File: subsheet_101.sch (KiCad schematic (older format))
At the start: 6 parts, among them U101 ST_BLITTER_PHY

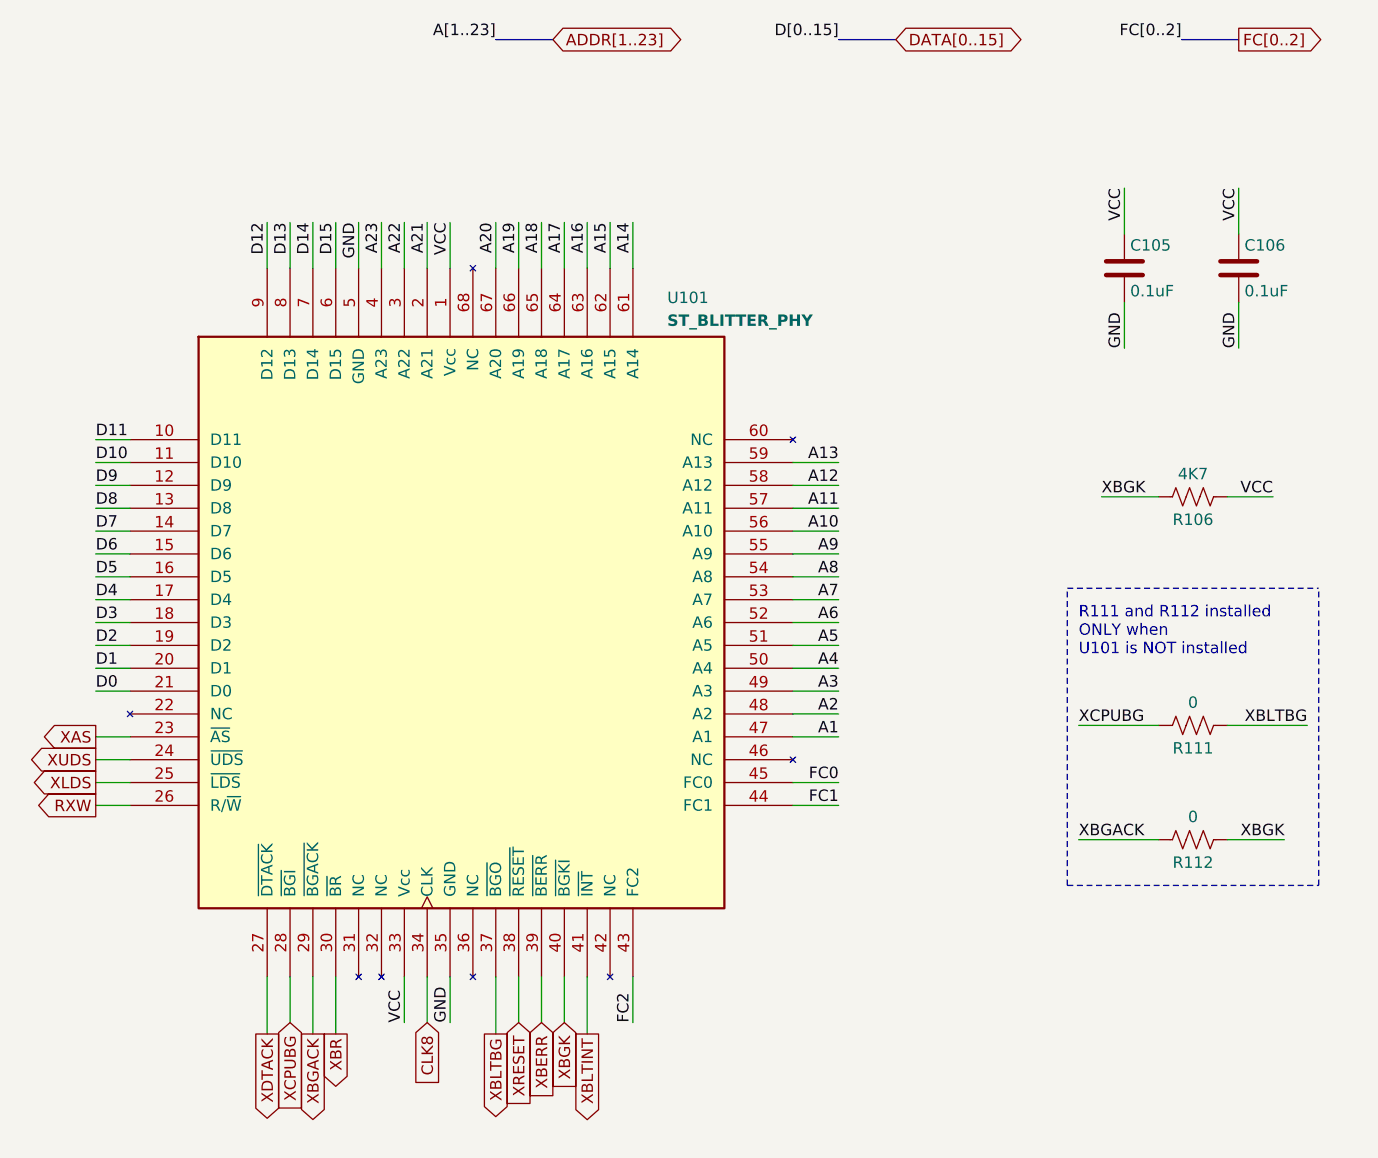
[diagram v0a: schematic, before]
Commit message: removed the external blitter
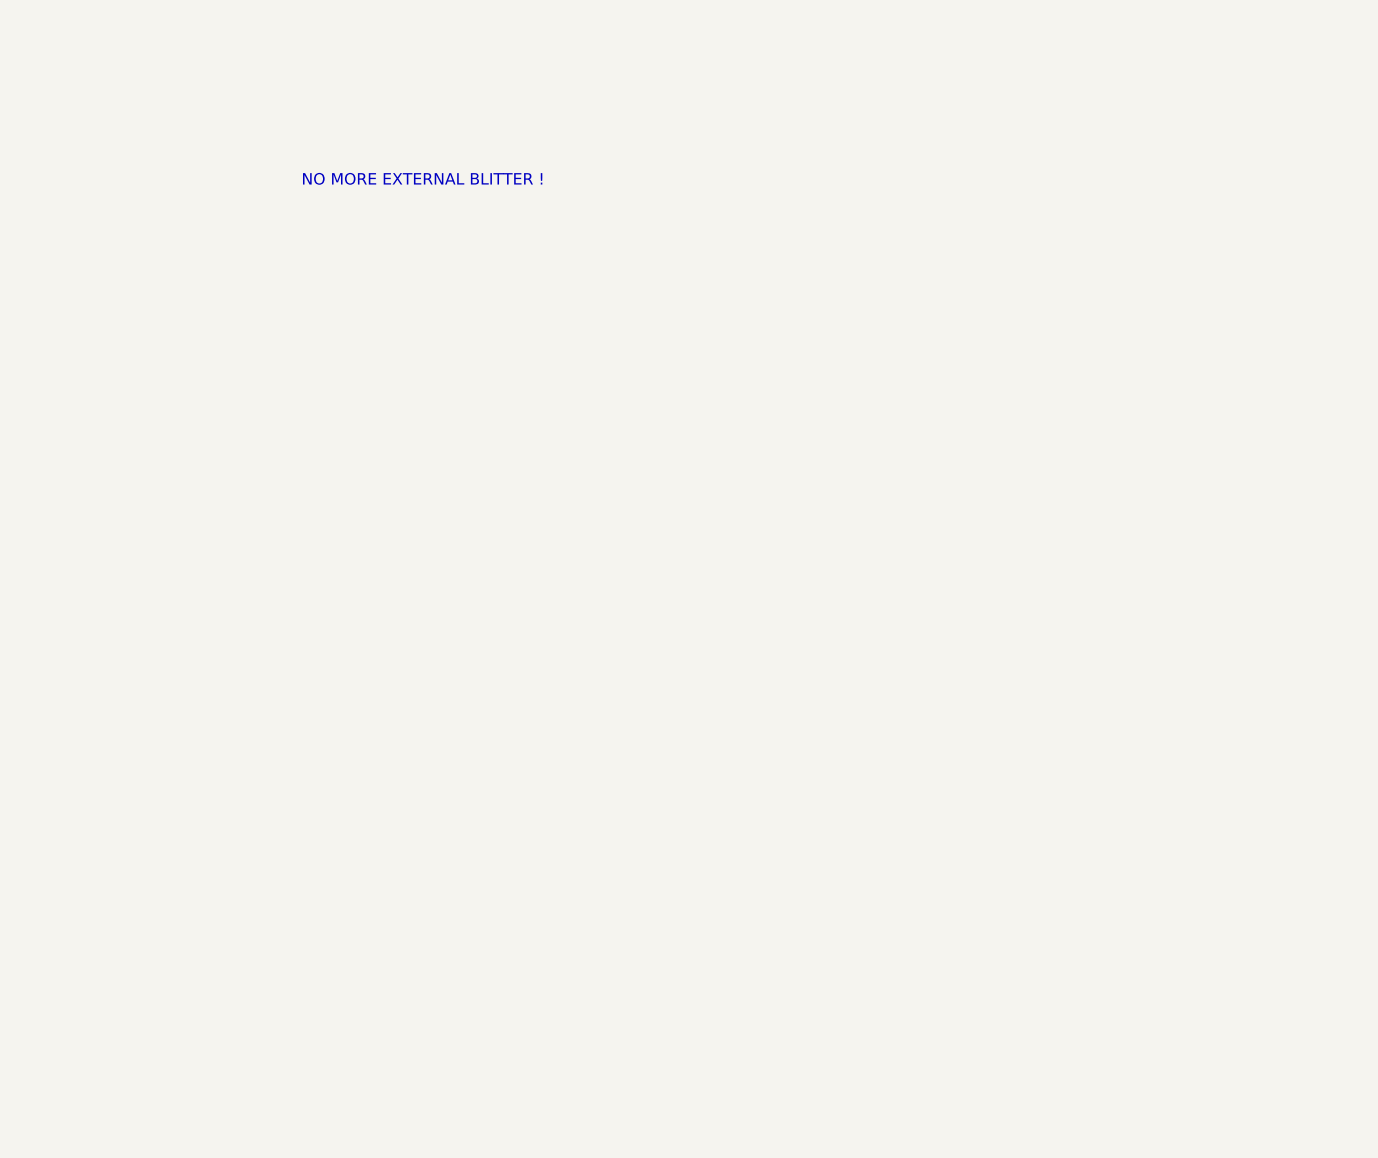
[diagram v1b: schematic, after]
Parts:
- removed C105, C106: 0.1uF, commons_passives_THT:Passive_THT_capacitor_mlcc_W2.54mm_L7.62mm, symbol Device:C
- removed R106: 4K7, commons_passives_THT:Passive_THT_resistor_W2.54mm_L12.70mm, symbol Device:R_US
- removed R111, R112: 0, commons_passives_THT:Passive_THT_resistor_W2.54mm_L12.70mm, symbol Device:R_US
- removed U101: ST_BLITTER_PHY, Package_LCC:PLCC-68_THT-Socket, symbol st_blitter:ST_BLITTER_PHY
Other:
- note added: "NO MORE EXTERNAL BLITTER !"
- note removed: "R111 and R112 installed\nONLY when \nU101 is NOT installed"

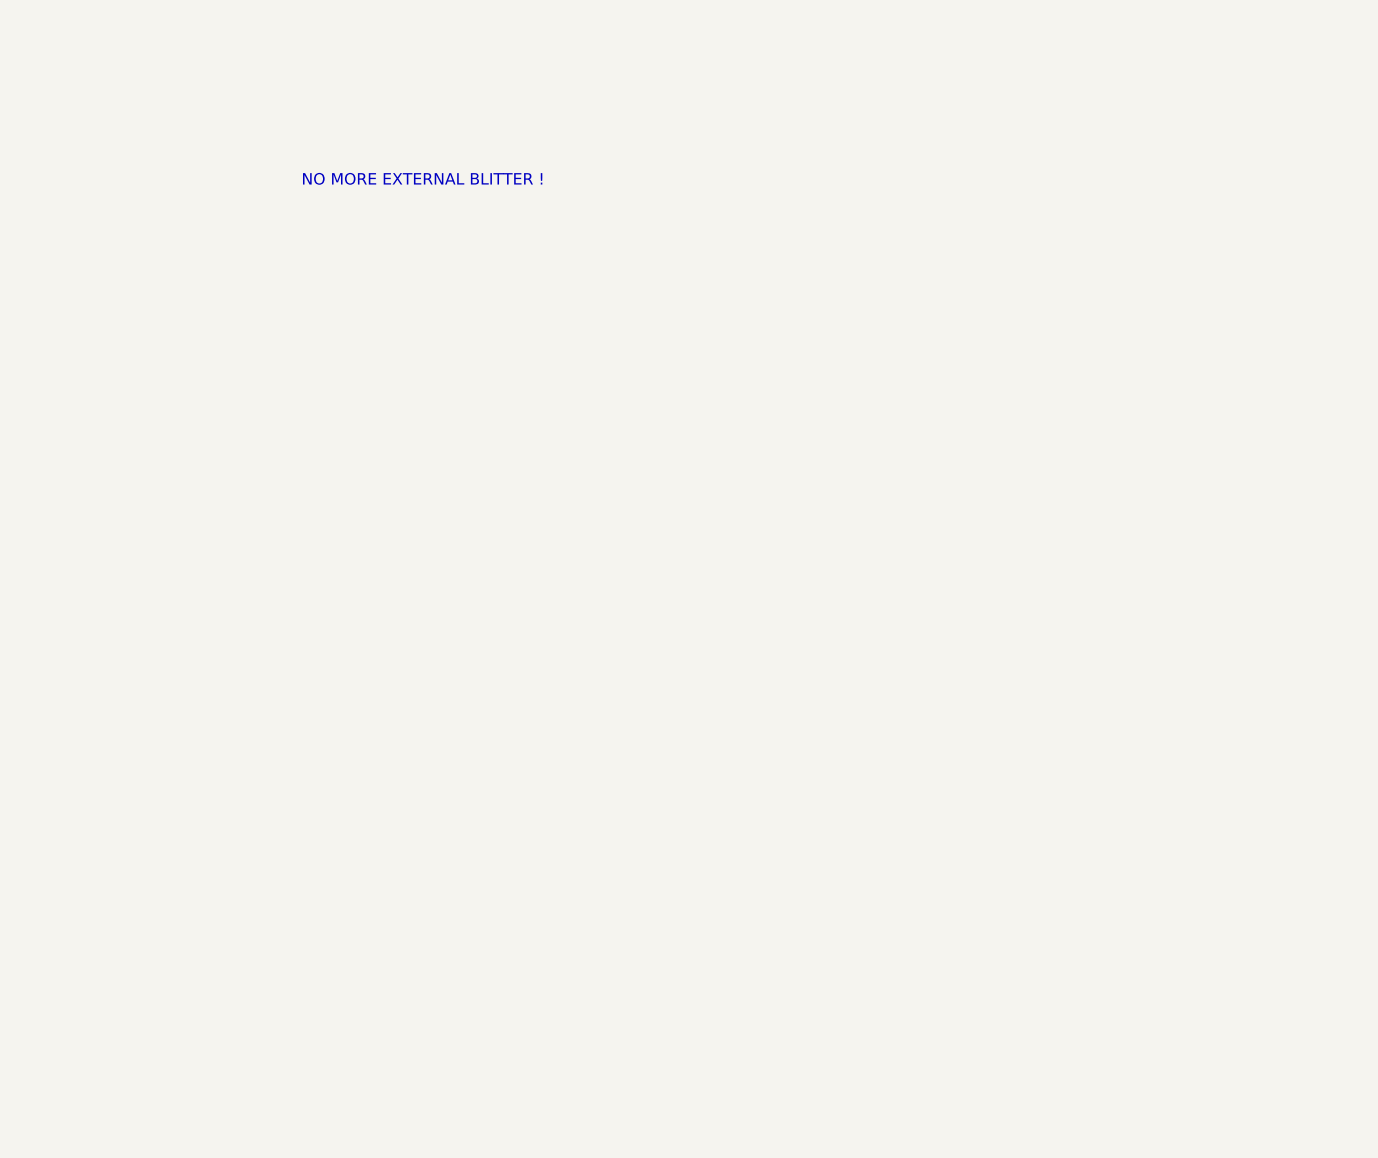
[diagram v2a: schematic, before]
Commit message: Fixes #19 : Reinstate the external blitter for the mark 0 version
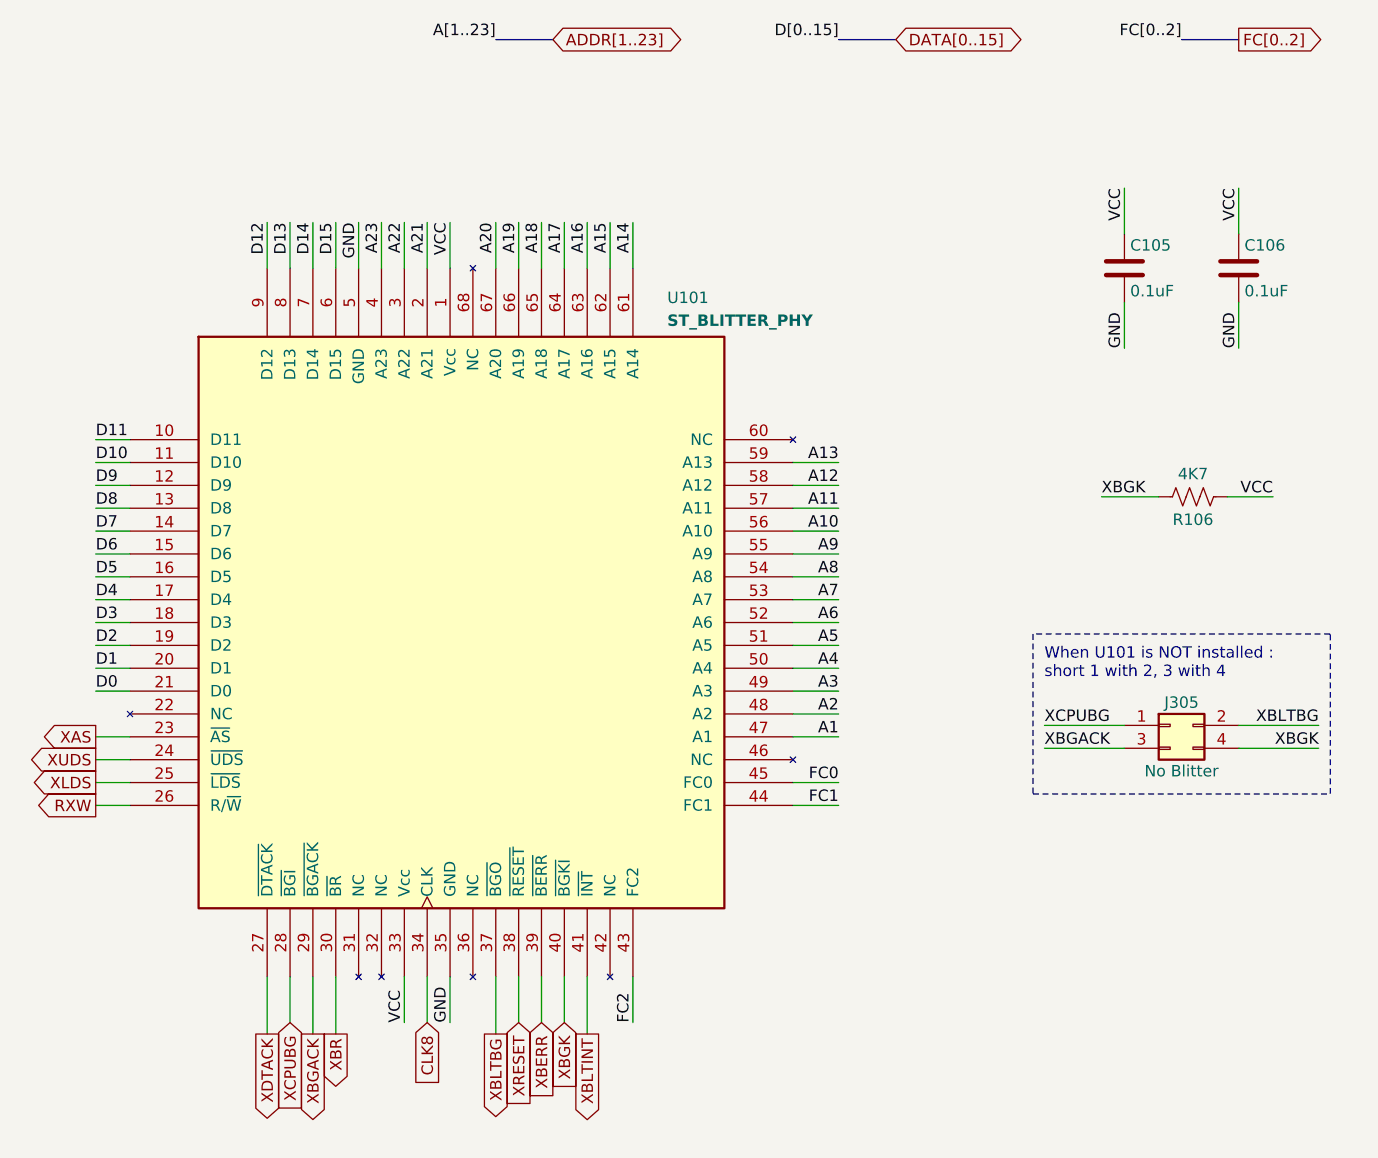
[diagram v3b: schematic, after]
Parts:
- added C105, C106: 0.1uF, commons_passives_THT:Passive_THT_capacitor_mlcc_W2.54mm_L7.62mm, symbol Device:C
- added J305: No Blitter, Connector_PinHeader_2.54mm:PinHeader_2x02_P2.54mm_Vertical, symbol Connector_Generic:Conn_02x02_Odd_Even
- added R106: 4K7, commons_passives_THT:Passive_THT_resistor_W2.54mm_L12.70mm, symbol Device:R_US
- added U101: ST_BLITTER_PHY, Package_LCC:PLCC-68_THT-Socket, symbol st_blitter:ST_BLITTER_PHY
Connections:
- new net A1: U101.47 (A1)
- new net A10: U101.56 (A10)
- new net A11: U101.57 (A11)
- new net A12: U101.58 (A12)
- new net A13: U101.59 (A13)
- new net A14: U101.61 (A14)
- new net A15: U101.62 (A15)
- new net A16: U101.63 (A16)
- new net A17: U101.64 (A17)
- new net A18: U101.65 (A18)
- new net A19: U101.66 (A19)
- new net A2: U101.48 (A2)
- new net A20: U101.67 (A20)
- new net A21: U101.2 (A21)
- new net A22: U101.3 (A22)
- new net A23: U101.4 (A23)
- new net A3: U101.49 (A3)
- new net A4: U101.50 (A4)
- new net A5: U101.51 (A5)
- new net A6: U101.52 (A6)
- new net A7: U101.53 (A7)
- new net A8: U101.54 (A8)
- new net A9: U101.55 (A9)
- new net CLK8: U101.34 (CLK)
- new net D0: U101.21 (D0)
- new net D1: U101.20 (D1)
- new net D10: U101.11 (D10)
- new net D11: U101.10 (D11)
- new net D12: U101.9 (D12)
- new net D13: U101.8 (D13)
- new net D14: U101.7 (D14)
- new net D15: U101.6 (D15)
- new net D2: U101.19 (D2)
- new net D3: U101.18 (D3)
- new net D4: U101.17 (D4)
- new net D5: U101.16 (D5)
- new net D6: U101.15 (D6)
- new net D7: U101.14 (D7)
- new net D8: U101.13 (D8)
- new net D9: U101.12 (D9)
- new net FC0: U101.45 (FC0)
- new net FC1: U101.44 (FC1)
- new net FC2: U101.43 (FC2)
- new net GND: C105.2, C106.2, U101.35 (GND), U101.5 (GND)
- new net RXW: U101.26 (R/~W~)
- new net VCC: C105.1, C106.1, R106.1, U101.1 (Vcc), U101.33 (Vcc)
- new net XAS: U101.23 (~AS~)
- new net XBERR: U101.39 (~BERR~)
- new net XBGACK: J305.3 (Pin_3), U101.29 (~BGACK~)
- new net XBGK: J305.4 (Pin_4), R106.2, U101.40 (~BGKI~)
- new net XBLTBG: J305.2 (Pin_2), U101.37 (~BGO~)
- new net XBLTINT: U101.41 (~INT~)
- new net XBR: U101.30 (~BR~)
- new net XCPUBG: J305.1 (Pin_1), U101.28 (~BGI~)
- new net XDTACK: U101.27 (~DTACK~)
- new net XLDS: U101.25 (~LDS~)
- new net XRESET: U101.38 (~RESET~)
- new net XUDS: U101.24 (~UDS~)
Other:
- note added: "When U101 is NOT installed :\nshort 1 with 2, 3 with 4"
- note removed: "NO MORE EXTERNAL BLITTER !"
